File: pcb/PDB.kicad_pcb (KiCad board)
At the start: 2 copper layers, 77.5 x 50.8 mm, 118 parts, among them J1 USB_C_Receptacle, J2 Conn_02x02_Counter_Clockwise, J3 Conn_02x02_Counter_Clockwise, J4 Conn_02x02_Counter_Clockwise, J5 Conn_02x02_Counter_Clockwise, J6 Conn_01x03_Pin, J7 Conn_01x03_Pin, SW1 SW_Push, SW2 SW_DIP_x02, U1 BD81870EFV-ME2, U10 LM337_TO252, U11 LM317_TO-252, U12 ATtiny1606-S, U13 FT230XS, U2 LM321, U3 L78L05_SOT89, U4 TL431DBZ, U5 INA181, U6 TL431DBZ, U7 INA181, U8 TL431DBZ, U9 INA181

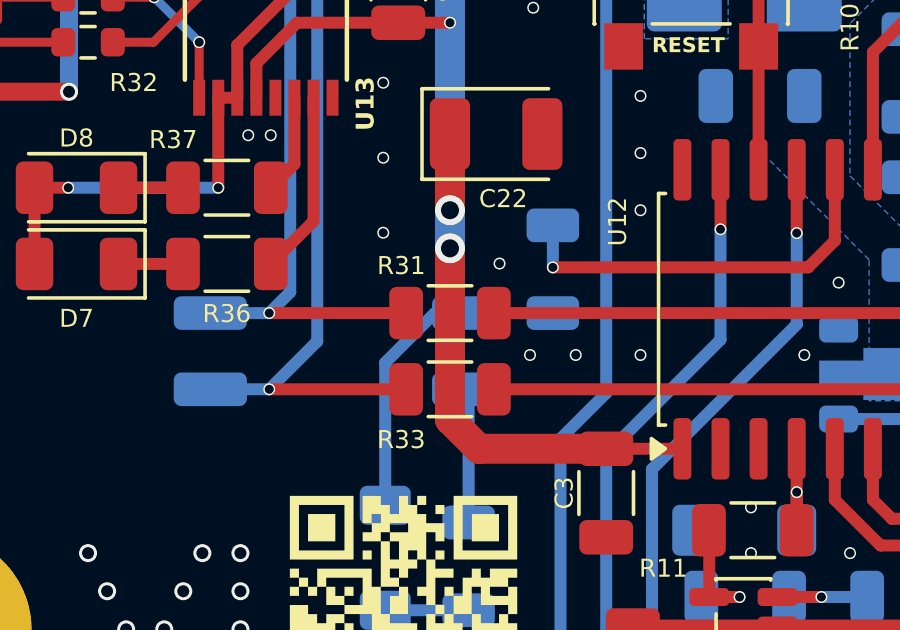
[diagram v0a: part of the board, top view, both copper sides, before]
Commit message: Modify voltage divider and silkscreen
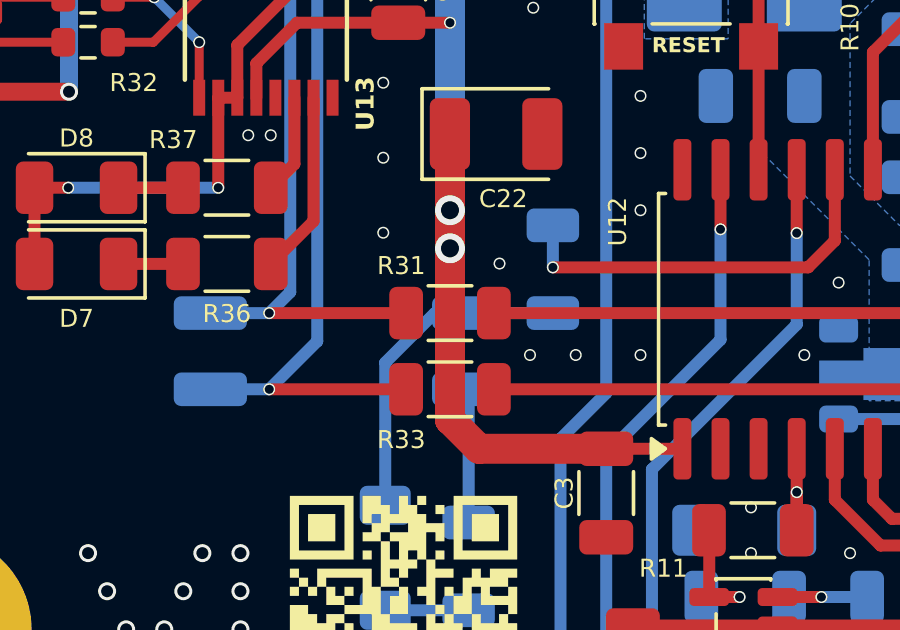
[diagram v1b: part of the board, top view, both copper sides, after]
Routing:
- net +5V: track 102.6 -> 109.6 mm
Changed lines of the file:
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@@
 		(tags "capacitor")
 		(property "Reference" "C13"
-			(at -0.0125 4.33 90)
+			(at -0.0125 -1.639 90)
 			(layer "B.SilkS")
 			(effects
@@
 		(tags "resistor")
 		(property "Reference" "R8"
-			(at 0 4.169 90)
+			(at 0 -1.419 90)
 			(layer "B.SilkS")
 			(effects
@@
 		(layer "F.Cu")
 		(net 2)
+	)
+	(segment
+		(start 141.605 107.95)
+		(end 141.605 114.935)
+		(width 1)
+		(layer "F.Cu")
+		(net 2)

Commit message: Update +15V voltage divider resistor values
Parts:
- R23: value 2k7 -> 1k8
- R24: value 750 -> 634
- R25: value 8k2 -> 5k1
- R26: value 8k2 -> 6k8
- R40: value 18k -> 6k8
- R43: value 6k8 -> 2k2
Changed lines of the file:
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@@
 			)
 		)
-		(property "Value" "8k2"
+		(property "Value" "5k1"
 			(at 3.2365 0 90)
 			(layer "F.Fab")
@@
 			)
 		)
-		(property "HTL" "102966"
+		(property "HTL" "102962"
 			(at 0 0 90)
 			(unlocked yes)
@@
 			)
 		)
-		(property "Value" "750"
+		(property "Value" "634"
 			(at 3.1095 0 0)
 			(layer "B.Fab")
@@
 			)
 		)
-		(property "HTL" "102949"
+		(property "HTL" "102947"
 			(at 0 0 180)
 			(unlocked yes)
@@
 			)
 		)
-		(property "Value" "2k7"
+		(property "Value" "1k8"
 			(at 0 -1.82 90)
 			(layer "B.Fab")
@@
 			)
 		)
-		(property "HTL" "102958"
+		(property "HTL" "102955"
 			(at 0 0 270)
 			(unlocked yes)
@@
 		(tags "resistor")
 		(property "Reference" "R40"
-			(at 0.3195 3.937 90)
+			(at 1.1325 -1.65 90)
 			(layer "B.SilkS")
 			(effects
@@
 			)
 		)
-		(property "Value" "18k"
+		(property "Value" "6k8"
 			(at 3.2405 0 90)
 			(layer "B.Fab")
@@
 			)
 		)
-		(property "HTL" "102971"
+		(property "HTL" "102964"
 			(at 0 0 270)
 			(unlocked yes)
@@
 		(tags "resistor")
 		(property "Reference" "R43"
-			(at -1.2085 4.191 90)
+			(at -0.3195 -1.397 90)
 			(layer "B.SilkS")
 			(effects
@@
 			)
 		)
-		(property "Value" "6k8"
+		(property "Value" "2k2"
 			(at -3.2405 0 90)
 			(layer "B.Fab")
@@
 			)
 		)
-		(property "HTL" "102964"
+		(property "HTL" "102956"
 			(at 0 0 90)
 			(unlocked yes)
@@
 			)
 		)
-		(property "Value" "8k2"
+		(property "Value" "6k8"
 			(at 0 -1.82 90)
 			(layer "B.Fab")
@@
 			)
 		)
-		(property "HTL" "102966"
+		(property "HTL" "102964"
 			(at 0 0 270)
 			(unlocked yes)
